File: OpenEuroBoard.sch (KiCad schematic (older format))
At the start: 124 parts, among them J1 Eurorack_bus_mini, J10 Jack, J11 Conn_01x08, J12 Jack, J13 Jack, J14 Jack, J15 Jack, J16 Conn_01x04, J17 MIDI_in, J18 Conn_01x03, J19 Conn_01x03, J2 Conn_01x07, J20 Conn_01x03, J21 MIDI_out, J22 Conn_01x03, J23 Conn_01x05, J24 Conn_01x03, J25 Conn_01x05, J26 Conn_01x03, J27 Conn_01x08, J28 Conn_01x08, J29 Conn_01x04, J3 Conn_01x07, J30 Screw_Terminal_01x01, J31 Conn_01x05, J32 Conn_01x03, J33 Conn_01x05, J34 Conn_01x03, J35 Conn_01x05, J36 Conn_01x03, J37 Screw_Terminal_01x01, J38 Screw_Terminal_01x01, J39 Conn_01x05, J4 Conn_01x07, J40 Conn_01x03, J41 Conn_01x03, J42 Conn_01x05, J43 Conn_01x03, J44 Conn_01x03, J45 Conn_01x02, J46 Conn_01x04, J47 Screw_Terminal_01x01, J48 Screw_Terminal_01x01, J49 Screw_Terminal_01x01, J5 Conn_01x07, J50 Screw_Terminal_01x01, J51 Screw_Terminal_01x01, J52 Conn_01x04, J53 Conn_01x04, J54 Conn_01x04, J6 Jack, J7 Jack, J8 Conn_01x08, J9 Jack, SW1 SW_Push, SW10 SW_SPDT, SW11 SW_SPDT, SW12 SW_SPDT, SW2 SW_Push, SW3 SW_Push, SW4 SW_Push, SW5 SW_Push, SW6 SW_Push, SW7 SW_SPDT, SW8 SW_SPDT, SW9 SW_SPDT, U1 LM1117IMP-5, U2 TL074, U3 TL074, U4 CD40107BE, U5 6N139, U6 TL074

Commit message: Silkscreen and general rework
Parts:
- added J55: Jumpers, Connector_PinHeader_2.54mm:PinHeader_2x05_P2.54mm_Vertical, symbol Connector_Generic:Conn_02x05_Top_Bottom
- added J?: Conn_01x04, Connector_PinHeader_2.54mm:PinHeader_1x04_P2.54mm_Vertical, symbol Connector_Generic:Conn_01x04
- added J?: Conn_01x08, Connector_PinHeader_2.54mm:PinHeader_1x08_P2.54mm_Vertical, symbol Connector_Generic:Conn_01x08
- J10: value Jack -> Jack 4
- J12: value Jack -> Jack 5
- J13: value Jack -> Jack 6
- J14: value Jack -> Jack 7
- J15: value Jack -> Jack 8
- J6: value Jack -> Jack 1
- J7: value Jack -> Jack 2
- J9: value Jack -> Jack 3
- RV3: value 1M LOG -> 1M
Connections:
- net +12V: now also J?.1 (Pin_1), J?.2 (Pin_2)
- net GND: now also J?.7 (Pin_7), J?.8 (Pin_8)
- new net TEST1: J?.1 (Pin_1), J?.3 (Pin_3)
- new net TEST2: J?.2 (Pin_2), J?.4 (Pin_4)
- new net TEST3: J?.3 (Pin_3), J?.5 (Pin_5)
- new net TEST4: J?.4 (Pin_4), J?.6 (Pin_6)
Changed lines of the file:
@@
 P 12300 6100
 F 0 "RV3" H 12232 6146 50  0000 R CNN
-F 1 "1M LOG" H 12232 6055 50  0000 R CNN
+F 1 "1M" H 12232 6055 50  0000 R CNN
 F 2 "w_pth_resistors:trimmer_alps-rk09k1130ah1" H 12300 6100 50  0001 C CNN
 F 3 "~" H 12300 6100 50  0001 C CNN
@@
 P 4300 3100
 F 0 "J6" H 4120 3033 50  0000 R CNN
-F 1 "Jack" H 4120 3124 50  0000 R CNN
+F 1 "Jack 1" H 4120 3124 50  0000 R CNN
 F 2 "SensaiLib:Thonkiconn Mono vertical minijack" H 4300 3100 50  0001 C CNN
 F 3 "~" H 4300 3100 50  0001 C CNN
@@
 P 5050 3100
 F 0 "J9" H 4870 3033 50  0000 R CNN
-F 1 "Jack" H 4870 3124 50  0000 R CNN
+F 1 "Jack 3" H 4870 3124 50  0000 R CNN
 F 2 "SensaiLib:Thonkiconn Mono vertical minijack" H 5050 3100 50  0001 C CNN
 F 3 "~" H 5050 3100 50  0001 C CNN
@@
 P 5800 3100
 F 0 "J12" H 5620 3033 50  0000 R CNN
-F 1 "Jack" H 5620 3124 50  0000 R CNN
+F 1 "Jack 5" H 5620 3124 50  0000 R CNN
 F 2 "SensaiLib:Thonkiconn Mono vertical minijack" H 5800 3100 50  0001 C CNN
 F 3 "~" H 5800 3100 50  0001 C CNN
@@
 P 6550 3100
 F 0 "J14" H 6370 3033 50  0000 R CNN
-F 1 "Jack" H 6370 3124 50  0000 R CNN
+F 1 "Jack 7" H 6370 3124 50  0000 R CNN
 F 2 "SensaiLib:Thonkiconn Mono vertical minijack" H 6550 3100 50  0001 C CNN
 F 3 "~" H 6550 3100 50  0001 C CNN
@@
 P 4300 3750
 F 0 "J7" H 4120 3683 50  0000 R CNN
-F 1 "Jack" H 4120 3774 50  0000 R CNN
+F 1 "Jack 2" H 4120 3774 50  0000 R CNN
 F 2 "SensaiLib:Thonkiconn Mono vertical minijack" H 4300 3750 50  0001 C CNN
 F 3 "~" H 4300 3750 50  0001 C CNN
@@
 P 5050 3750
 F 0 "J10" H 4870 3683 50  0000 R CNN
-F 1 "Jack" H 4870 3774 50  0000 R CNN
+F 1 "Jack 4" H 4870 3774 50  0000 R CNN
 F 2 "SensaiLib:Thonkiconn Mono vertical minijack" H 5050 3750 50  0001 C CNN
 F 3 "~" H 5050 3750 50  0001 C CNN
@@
 P 5800 3750
 F 0 "J13" H 5620 3683 50  0000 R CNN
-F 1 "Jack" H 5620 3774 50  0000 R CNN
+F 1 "Jack 6" H 5620 3774 50  0000 R CNN
 F 2 "SensaiLib:Thonkiconn Mono vertical minijack" H 5800 3750 50  0001 C CNN
 F 3 "~" H 5800 3750 50  0001 C CNN
@@
 P 6550 3750
 F 0 "J15" H 6370 3683 50  0000 R CNN
-F 1 "Jack" H 6370 3774 50  0000 R CNN
+F 1 "Jack 8" H 6370 3774 50  0000 R CNN
 F 2 "SensaiLib:Thonkiconn Mono vertical minijack" H 6550 3750 50  0001 C CNN
 F 3 "~" H 6550 3750 50  0001 C CNN
@@
 Wire Wire Line
 	7750 6750 7750 6600
+$Comp
+L Connector_Generic:Conn_02x05_Top_Bottom J55
+U 1 1 5F3DB406
+P 4150 7200
+F 0 "J55" H 4200 7617 50  0000 C CNN
+F 1 "Jumpers" H 4200 7526 50  0000 C CNN
+F 2 "Connector_PinHeader_2.54mm:PinHeader_2x05_P2.54mm_Vertical" H 4150 7200 50  0001 C CNN
+F 3 "~" H 4150 7200 50  0001 C CNN
+	1    4150 7200
+	1    0    0    -1
+$EndComp
+$Comp
+L Connector_Generic:Conn_01x04 J?
+U 1 1 5F41DDFC
+P 5800 7200
+F 0 "J?" V 5766 6912 50  0000 R CNN
+F 1 "Conn_01x04" V 5675 6912 50  0000 R CNN
+F 2 "Connector_PinHeader_2.54mm:PinHeader_1x04_P2.54mm_Vertical" H 5800 7200 50  0001 C CNN
+F 3 "~" H 5800 7200 50  0001 C CNN
+	1    5800 7200
+	1    0    0    -1
+$EndComp
+Text GLabel 5600 7100 0    50   Input ~ 0
+TEST1
+Text GLabel 5600 7200 0    50   Input ~ 0
+TEST2
+Text GLabel 5600 7400 0    50   Input ~ 0
+TEST4
+Text GLabel 5600 7300 0    50   Input ~ 0
+TEST3
+$Comp
+L Connector_Generic:Conn_01x08 J?
+U 1 1 5F5E8658
+P 6700 7200
+F 0 "J?" V 6800 7550 50  0000 C CNN
+F 1 "Conn_01x08" V 6826 7146 50  0000 C CNN
+F 2 "Connector_PinHeader_2.54mm:PinHeader_1x08_P2.54mm_Vertical" H 6700 7200 50  0001 C CNN
+F 3 "~" H 6700 7200 50  0001 C CNN
+	1    6700 7200
+	1    0    0    -1
+$EndComp
+Text GLabel 6500 7100 0    50   Input ~ 0
+TEST1
+Text GLabel 6500 7200 0    50   Input ~ 0
+TEST2
+Text GLabel 6500 7400 0    50   Input ~ 0
+TEST4
+Text GLabel 6500 7300 0    50   Input ~ 0
+TEST3
+$Comp
+L power:+12V #PWR?
+U 1 1 5F7B1B41
+P 6350 6900
+F 0 "#PWR?" H 6350 6750 50  0001 C CNN
+F 1 "+12V" H 6350 7150 50  0000 C CNN
+F 2 "" H 6350 6900 50  0001 C CNN
+F 3 "" H 6350 6900 50  0001 C CNN
+	1    6350 6900
+	0    -1   -1   0
+$EndComp
+Wire Wire Line
+	6350 6900 6500 6900
+$Comp
+L power:+12V #PWR?
+U 1 1 5F8B74FB
+P 6350 7000
+F 0 "#PWR?" H 6350 6850 50  0001 C CNN
+F 1 "+12V" H 6350 7250 50  0000 C CNN
+F 2 "" H 6350 7000 50  0001 C CNN
+F 3 "" H 6350 7000 50  0001 C CNN
+	1    6350 7000
+	0    -1   -1   0
+$EndComp
+Wire Wire Line
+	6350 7000 6500 7000
+$Comp
+L power:GND #PWR?
+U 1 1 5F9BE033
+P 6250 7650
+F 0 "#PWR?" H 6250 7400 50  0001 C CNN
+F 1 "GND" H 6250 7400 50  0000 C CNN
+F 2 "" H 6250 7650 50  0001 C CNN
+F 3 "" H 6250 7650 50  0001 C CNN
+	1    6250 7650
+	1    0    0    -1
+$EndComp
+Wire Wire Line
+	6500 7600 6250 7600
+Wire Wire Line
+	6250 7600 6250 7650
+Wire Wire Line
+	6250 7500 6250 7600
+Connection ~ 6250 7600
+Wire Wire Line
+	6250 7500 6500 7500
 $EndSCHEMATC

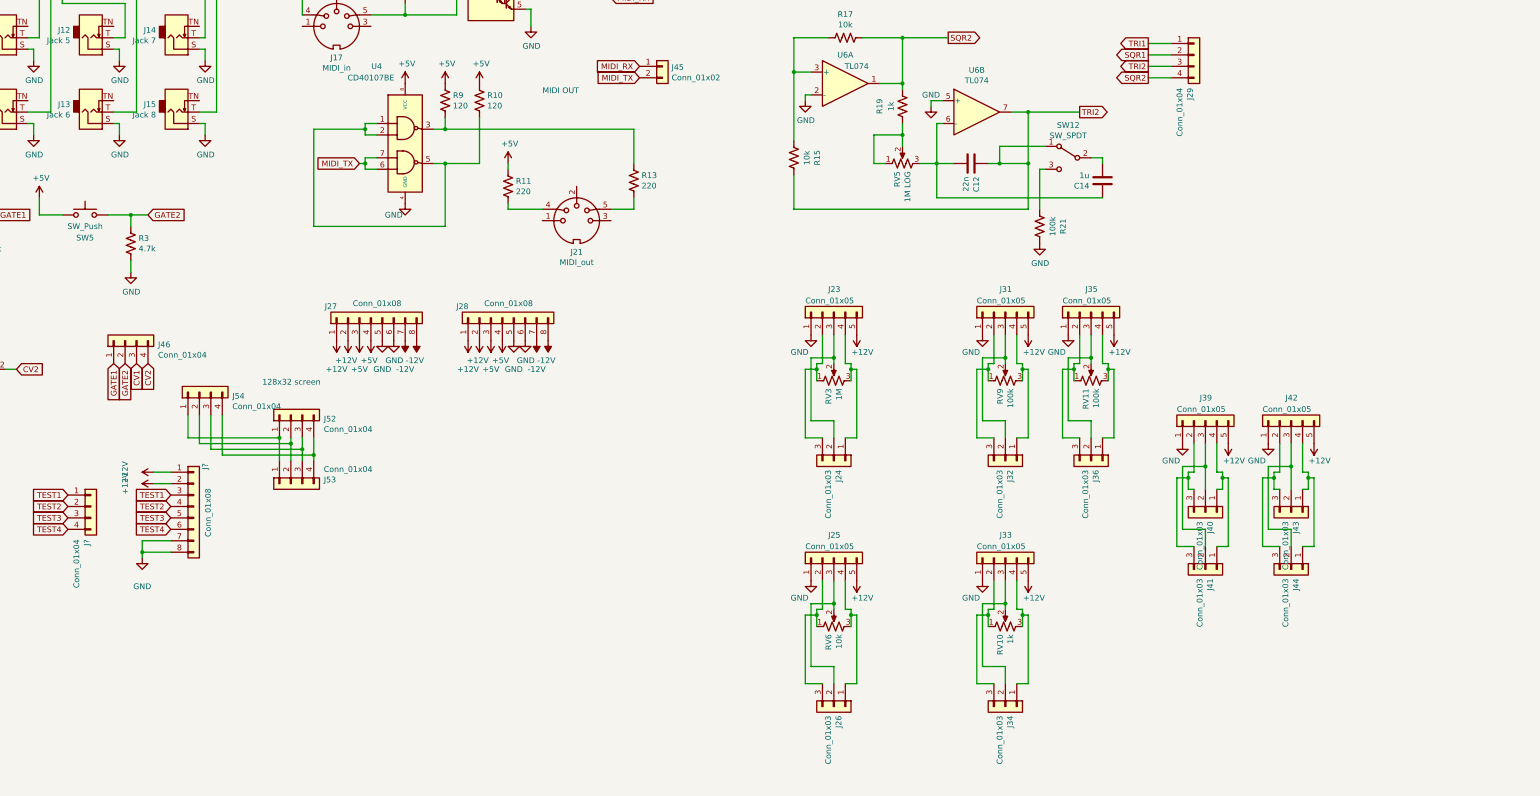
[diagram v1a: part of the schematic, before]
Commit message: Finished layout, silkscreen and routing
also fixed minijack footprint
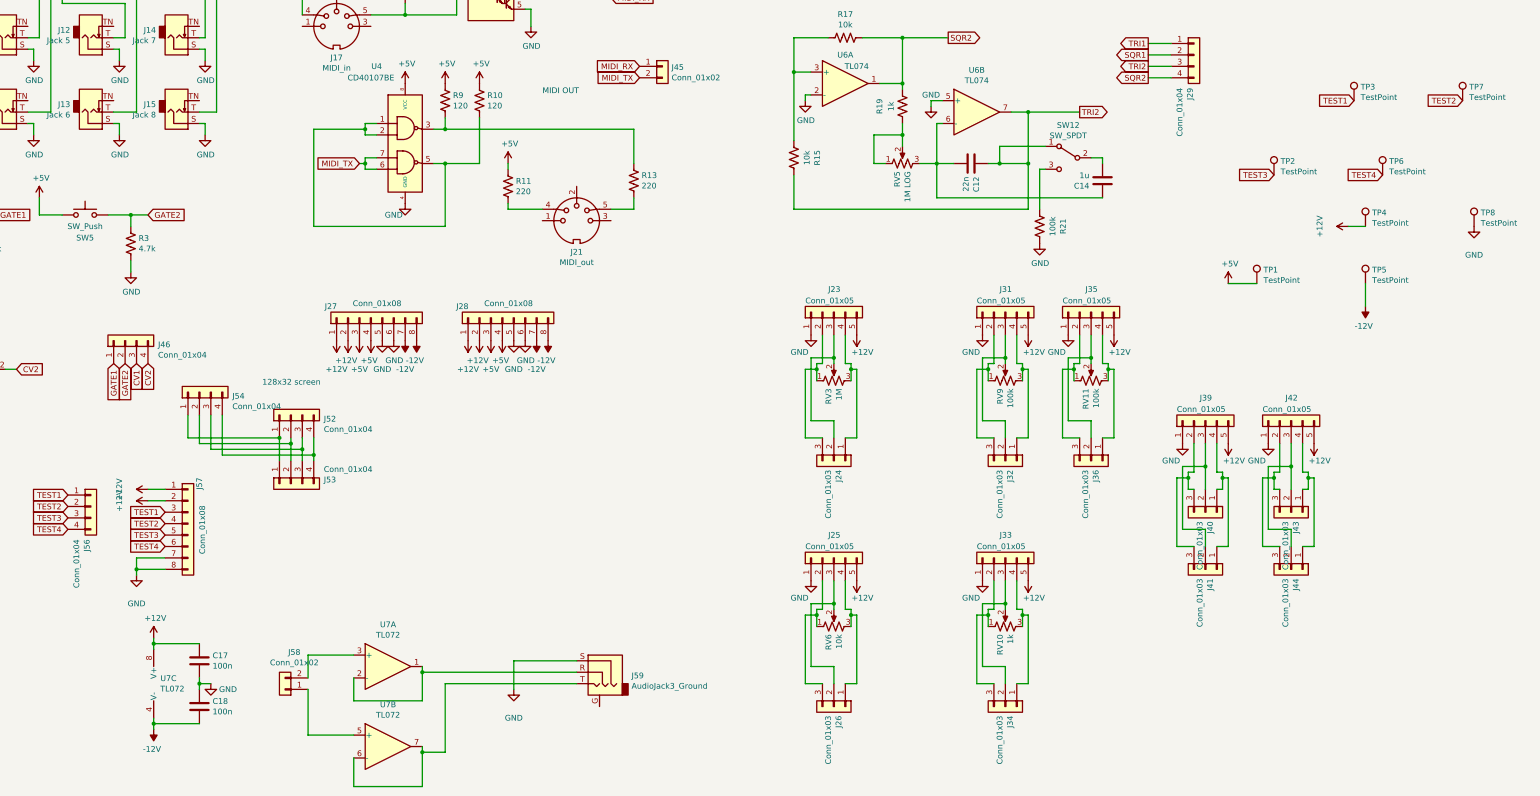
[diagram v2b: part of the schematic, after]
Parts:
- added C17, C18: 100n, Capacitor_THT:C_Disc_D3.4mm_W2.1mm_P2.50mm, symbol Device:C
- added J58: Conn_01x02, Connector_PinHeader_2.54mm:PinHeader_1x02_P2.54mm_Vertical, symbol Connector_Generic:Conn_01x02
- added J59: AudioJack3_Ground, SensaiLib:Jack Stereo vertical Thonk, symbol Connector:AudioJack3_Ground
- added TP1, TP2, TP3, TP4, TP5, TP6, TP7, TP8: TestPoint, TestPoint:TestPoint_THTPad_D3.0mm_Drill1.5mm, symbol Connector:TestPoint
- added U7: TL072, Package_DIP:DIP-8_W7.62mm_Socket_LongPads, symbol Amplifier_Operational:TL072
- gave numbers to parts that had none: 2
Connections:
- net +12V: now also C17.1, TP4.1, U7.8 (V+)
- net +5V: now also TP1.1
- net -12V: now also C18.2, TP5.1, U7.4 (V-)
- net GND: now also C17.2, C18.1, J59.S, TP8.1
- net TEST1: now also TP3.1
- net TEST2: now also TP7.1
- net TEST3: now also TP2.1
- net TEST4: now also TP6.1
- new net: J58.1 (Pin_1), U7.5 (+)
- new net: J58.2 (Pin_2), U7.3 (+)
- new net: J59.R, U7.1, U7.2 (-)
- new net: J59.T, U7.6 (-), U7.7
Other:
- moved on the sheet: J57

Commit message: stuff
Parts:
- J10, J12, J13, J14, J15, J6, J7, J9: footprint SensaiLib:Thonkiconn Mono vertical minijack -> Connector_Audio:Jack_3.5mm_QingPu_WQP-PJ398SM_Vertical_CircularHoles
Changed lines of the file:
@@
 F 0 "J6" H 4120 3033 50  0000 R CNN
 F 1 "Jack 1" H 4120 3124 50  0000 R CNN
-F 2 "SensaiLib:Thonkiconn Mono vertical minijack" H 4300 3100 50  0001 C CNN
+F 2 "Connector_Audio:Jack_3.5mm_QingPu_WQP-PJ398SM_Vertical_CircularHoles" H 4300 3100 50  0001 C CNN
 F 3 "~" H 4300 3100 50  0001 C CNN
 	1    4300 3100
@@
 F 0 "J9" H 4870 3033 50  0000 R CNN
 F 1 "Jack 3" H 4870 3124 50  0000 R CNN
-F 2 "SensaiLib:Thonkiconn Mono vertical minijack" H 5050 3100 50  0001 C CNN
+F 2 "Connector_Audio:Jack_3.5mm_QingPu_WQP-PJ398SM_Vertical_CircularHoles" H 5050 3100 50  0001 C CNN
 F 3 "~" H 5050 3100 50  0001 C CNN
 	1    5050 3100
@@
 F 0 "J12" H 5620 3033 50  0000 R CNN
 F 1 "Jack 5" H 5620 3124 50  0000 R CNN
-F 2 "SensaiLib:Thonkiconn Mono vertical minijack" H 5800 3100 50  0001 C CNN
+F 2 "Connector_Audio:Jack_3.5mm_QingPu_WQP-PJ398SM_Vertical_CircularHoles" H 5800 3100 50  0001 C CNN
 F 3 "~" H 5800 3100 50  0001 C CNN
 	1    5800 3100
@@
 F 0 "J14" H 6370 3033 50  0000 R CNN
 F 1 "Jack 7" H 6370 3124 50  0000 R CNN
-F 2 "SensaiLib:Thonkiconn Mono vertical minijack" H 6550 3100 50  0001 C CNN
+F 2 "Connector_Audio:Jack_3.5mm_QingPu_WQP-PJ398SM_Vertical_CircularHoles" H 6550 3100 50  0001 C CNN
 F 3 "~" H 6550 3100 50  0001 C CNN
 	1    6550 3100
@@
 F 0 "J7" H 4120 3683 50  0000 R CNN
 F 1 "Jack 2" H 4120 3774 50  0000 R CNN
-F 2 "SensaiLib:Thonkiconn Mono vertical minijack" H 4300 3750 50  0001 C CNN
+F 2 "Connector_Audio:Jack_3.5mm_QingPu_WQP-PJ398SM_Vertical_CircularHoles" H 4300 3750 50  0001 C CNN
 F 3 "~" H 4300 3750 50  0001 C CNN
 	1    4300 3750
@@
 F 0 "J10" H 4870 3683 50  0000 R CNN
 F 1 "Jack 4" H 4870 3774 50  0000 R CNN
-F 2 "SensaiLib:Thonkiconn Mono vertical minijack" H 5050 3750 50  0001 C CNN
+F 2 "Connector_Audio:Jack_3.5mm_QingPu_WQP-PJ398SM_Vertical_CircularHoles" H 5050 3750 50  0001 C CNN
 F 3 "~" H 5050 3750 50  0001 C CNN
 	1    5050 3750
@@
 F 0 "J13" H 5620 3683 50  0000 R CNN
 F 1 "Jack 6" H 5620 3774 50  0000 R CNN
-F 2 "SensaiLib:Thonkiconn Mono vertical minijack" H 5800 3750 50  0001 C CNN
+F 2 "Connector_Audio:Jack_3.5mm_QingPu_WQP-PJ398SM_Vertical_CircularHoles" H 5800 3750 50  0001 C CNN
 F 3 "~" H 5800 3750 50  0001 C CNN
 	1    5800 3750
@@
 F 0 "J15" H 6370 3683 50  0000 R CNN
 F 1 "Jack 8" H 6370 3774 50  0000 R CNN
-F 2 "SensaiLib:Thonkiconn Mono vertical minijack" H 6550 3750 50  0001 C CNN
+F 2 "Connector_Audio:Jack_3.5mm_QingPu_WQP-PJ398SM_Vertical_CircularHoles" H 6550 3750 50  0001 C CNN
 F 3 "~" H 6550 3750 50  0001 C CNN
 	1    6550 3750
